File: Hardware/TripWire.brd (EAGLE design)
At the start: 32.3 x 50.2 mm, 56 parts, among them P1 LSP11, P2 LSP11, P3 LSP11, P4 LSP11, P5 LSP11, P6 LSP11, P7 LSP11, X1 GADGETEER-SOCKET

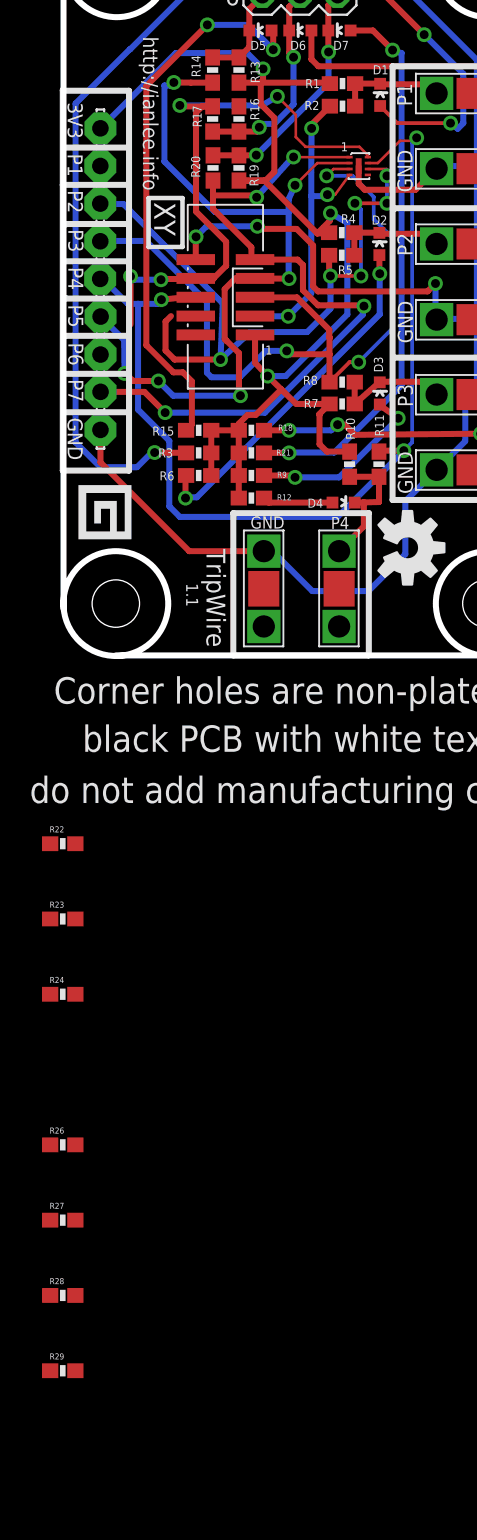
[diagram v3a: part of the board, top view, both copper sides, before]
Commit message: Started replacing TVS with BAT54S diode arrays.
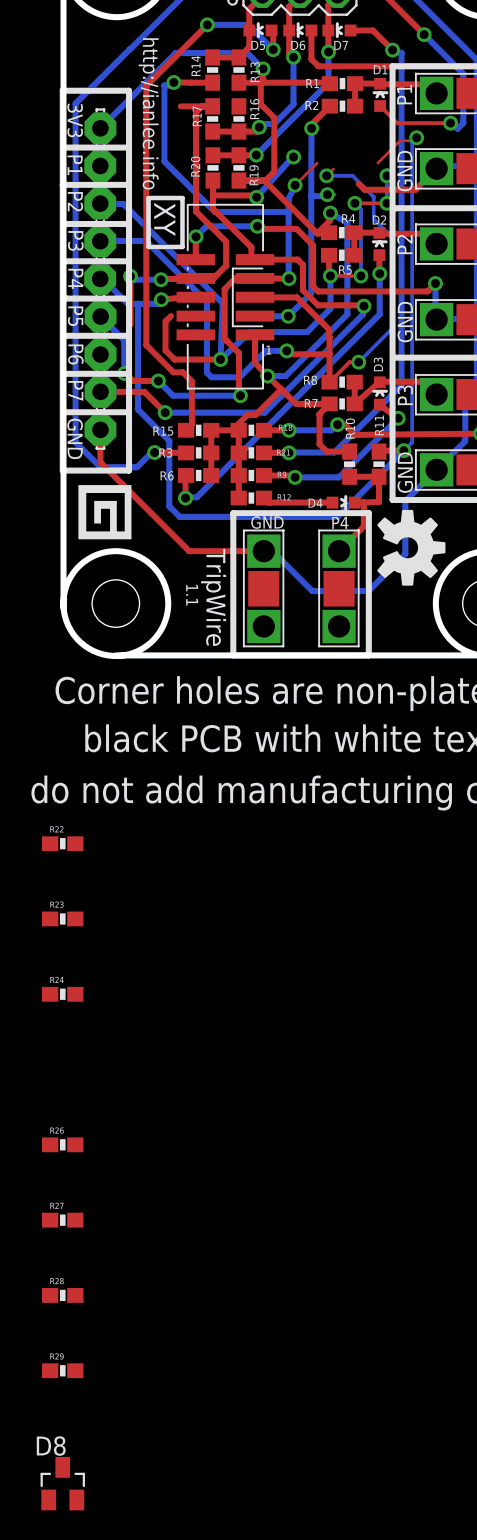
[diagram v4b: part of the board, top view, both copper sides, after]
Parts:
- removed VESD05A8A-HNH-GS08: VESD05A8A-HNH-GS088-UFDFN_TVS-DIODE-ARRAY, SoftDust:8-UFDFN
- added D8: BAT54S, diode:SOT23
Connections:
- net 3V3: now also D8.2
- net GND: now also D8.1; no longer VESD05A8A-HNH-GS08.P$9
- net PIN3: now also D8.3; no longer VESD05A8A-HNH-GS08.P$4
- net PIN4: no longer VESD05A8A-HNH-GS08.P$6
- net PIN5: no longer VESD05A8A-HNH-GS08.P$3
- net PIN6: no longer VESD05A8A-HNH-GS08.P$7
- net PIN7: no longer VESD05A8A-HNH-GS08.P$2
- net PIN8: no longer VESD05A8A-HNH-GS08.P$8
- net PIN9: no longer VESD05A8A-HNH-GS08.P$1
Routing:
- net PIN8: track 41.5 -> 26.0 mm, vias 4 -> 2
- net PIN9: track 16.6 -> 12.9 mm
- net PIN7: track 31.2 -> 29.1 mm
- net PIN3: track 21.2 -> 19.5 mm
- net PIN4: track 46.5 -> 45.3 mm
- net GND: track 117.0 -> 115.8 mm
- net PIN5: track 53.0 -> 52.0 mm
- net PIN6: track 66.7 -> 66.0 mm
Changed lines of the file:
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@@
 <attribute name="VALUE" x="2.295" y="17.7838" size="0.0254" layer="27" rot="R90"/>
 </element>
-<element name="VESD05A8A-HNH-GS08" library="SoftDust" package="8-UFDFN" value="VESD05A8A-HNH-GS088-UFDFN_TVS-DIODE-ARRAY" x="19.9644" y="33.02" smashed="yes"/>
 <element name="LOGO1" library="SparkFun-Aesthetics" package="OSHW-LOGO-M" value="OSHW-LOGOM" x="23.2664" y="7.2644" rot="R270"/>
 <element name="R22" library="SparkFun-Resistors" package="0603-RES" value="10" x="0" y="-12.7"/>
@@
 <element name="R28" library="SparkFun-Resistors" package="0603-RES" value="10" x="0" y="-43.18"/>
 <element name="R29" library="SparkFun-Resistors" package="0603-RES" value="10" x="0" y="-48.26"/>
+<element name="D8" library="diode" package="SOT23" value="BAT54S" x="0" y="-55.88"/>
 </elements>
 <signals>
@@
 <wire x1="13.02035" y1="16.2306" x2="14.7412875" y2="17.9515375" width="0.4064" layer="1"/>
 <wire x1="13.3604" y1="38.647" x2="13.3604" y2="37.1856" width="0.4064" layer="1"/>
+<contactref element="D8" pad="2"/>
+<wire x1="11.8754" y1="10.6172" x2="0.95" y2="-56.98" width="0" layer="19" extent="1-1"/>
 </signal>
 <signal name="GND" class="1">
@@
 <contactref element="SV1" pad="3"/>
 <contactref element="SV1" pad="1"/>
-<contactref element="VESD05A8A-HNH-GS08" pad="P$9"/>
 <wire x1="23.7998" y1="31.4198" x2="25.2222" y2="32.8422" width="0.4064" layer="1"/>
 <wire x1="21.082" y1="47.037" x2="18.542" y2="47.037" width="0.4064" layer="16"/>
@@
 <wire x1="25.2222" y1="22.6568" x2="25.273" y2="22.7076" width="0.4064" layer="16"/>
 <wire x1="25.273" y1="22.7076" x2="27.94" y2="22.7076" width="0.4064" layer="16"/>
-<wire x1="19.9644" y1="33.02" x2="19.9644" y2="31.8262" width="0.4064" layer="1"/>
 <wire x1="19.9644" y1="31.8262" x2="20.3708" y2="31.4198" width="0.4064" layer="1"/>
 <wire x1="20.3708" y1="31.4198" x2="23.7998" y2="31.4198" width="0.4064" layer="1"/>
 <wire x1="25.2222" y1="22.6568" x2="25.146" y2="22.6568" width="0.4064" layer="16"/>
-<wire x1="25.2476" y1="32.8676" x2="25.2222" y2="32.8422" width="0" layer="19" extent="16-16"/>
+<contactref element="D8" pad="1"/>
+<wire x1="16.8402" y1="4.3434" x2="-0.95" y2="-56.98" width="0" layer="19" extent="1-16"/>
+<wire x1="25.2222" y1="32.8422" x2="25.2476" y2="32.8676" width="0" layer="19" extent="16-16"/>
 </signal>
 <signal name="PIN3">
@@
 <wire x1="15.2146" y1="22.8854" x2="15.2038" y2="22.8962" width="0.4064" layer="1"/>
 <wire x1="12.6734" y1="22.8854" x2="15.2146" y2="22.8854" width="0.4064" layer="16"/>
-<contactref element="VESD05A8A-HNH-GS08" pad="P$4"/>
 <via x="17.8562" y="31.0896" extent="1-16" drill="0.6" shape="square"/>
 <wire x1="17.8562" y1="31.0896" x2="17.7546" y2="30.988" width="0.4064" layer="16"/>
 <wire x1="17.7546" y1="30.988" x2="16.764" y2="30.988" width="0.4064" layer="16"/>
 <wire x1="18.3736" y1="31.0896" x2="17.8562" y2="31.0896" width="0.1778" layer="1"/>
-<wire x1="19.3484" y1="32.42" x2="18.3736" y2="31.0896" width="0.1778" layer="1"/>
 <contactref element="R26" pad="1"/>
-<wire x1="-0.85" y1="-33.02" x2="12.6734" y2="22.8854" width="0" layer="19" extent="1-16"/>
+<contactref element="D8" pad="3"/>
+<wire x1="-0.85" y1="-33.02" x2="0" y2="-54.78" width="0" layer="19" extent="1-1"/>
+<wire x1="12.6734" y1="22.8854" x2="-0.85" y2="-33.02" width="0" layer="19" extent="1-16"/>
 </signal>
 <signal name="PIN4">
@@
 <wire x1="16.4846" y1="21.8186" x2="18.0594" y2="23.3934" width="0.4064" layer="16"/>
 <wire x1="18.0594" y1="23.3934" x2="18.0594" y2="25.6032" width="0.4064" layer="16"/>
-<contactref element="VESD05A8A-HNH-GS08" pad="P$6"/>
-<wire x1="20.5844" y1="32.82" x2="21.8662" y2="32.82" width="0.1778" layer="1"/>
 <wire x1="21.8662" y1="32.82" x2="21.8694" y2="32.3596" width="0.1778" layer="1"/>
 <via x="21.8694" y="32.3596" extent="1-16" drill="0.6" shape="square"/>
@@
 <wire x1="17.9832" y1="21.971" x2="17.9832" y2="21.4612" width="0.4064" layer="1"/>
 <wire x1="17.9832" y1="21.4612" x2="18.0086" y2="21.4358" width="0.4064" layer="1"/>
-<contactref element="VESD05A8A-HNH-GS08" pad="P$3"/>
-<wire x1="19.3484" y1="32.82" x2="18.2658" y2="32.82" width="0.1778" layer="1"/>
 <wire x1="18.2658" y1="32.82" x2="17.8054" y2="32.3596" width="0.1778" layer="1"/>
 <via x="17.8054" y="32.3596" extent="1-16" drill="0.6" shape="square"/>
@@
 <wire x1="15.2654" y1="25.4254" x2="12.9836" y2="25.4254" width="0.4064" layer="1"/>
 <wire x1="15.2654" y1="25.4254" x2="15.24" y2="25.4508" width="0.4064" layer="16"/>
-<contactref element="VESD05A8A-HNH-GS08" pad="P$2"/>
-<wire x1="19.3484" y1="33.22" x2="17.1672" y2="33.22" width="0.1778" layer="1"/>
 <via x="15.6718" y="31.7246" extent="1-16" drill="0.6" shape="square"/>
 <wire x1="15.24" y1="25.4508" x2="15.24" y2="29.9212" width="0.4064" layer="16"/>
@@
 <wire x1="10.1346" y1="30.1244" x2="12.7254" y2="27.5336" width="0.4064" layer="1"/>
 <wire x1="12.7254" y1="27.5336" x2="12.7254" y2="26.9536" width="0.4064" layer="1"/>
-<contactref element="VESD05A8A-HNH-GS08" pad="P$1"/>
-<wire x1="19.3484" y1="33.62" x2="15.5798" y2="33.62" width="0.1778" layer="1"/>
 <wire x1="15.5798" y1="33.62" x2="15.5702" y2="33.6296" width="0.4064" layer="1"/>
 <via x="15.5702" y="33.6296" extent="1-16" drill="0.6" shape="square"/>
@@
 <wire x1="7.1882" y1="14.478" x2="5.08" y2="16.5862" width="0.4064" layer="16"/>
 <wire x1="5.08" y1="16.5862" x2="5.08" y2="23.7236" width="0.4064" layer="16"/>
-<contactref element="VESD05A8A-HNH-GS08" pad="P$7"/>
-<wire x1="20.5844" y1="33.22" x2="21.2566" y2="33.22" width="0.1778" layer="1"/>
 <wire x1="21.2566" y1="33.22" x2="22.7584" y2="34.7218" width="0.1778" layer="1"/>
 <wire x1="22.7584" y1="34.7218" x2="23.5458" y2="34.7218" width="0.1778" layer="1"/>
@@
 <wire x1="4.8006" y1="25.3492" x2="6.6294" y2="25.3492" width="0.4064" layer="16"/>
 <wire x1="4.572" y1="22.324" x2="4.572" y2="25.5778" width="0.4064" layer="1"/>
-<contactref element="VESD05A8A-HNH-GS08" pad="P$8"/>
-<via x="14.478" y="37.719" extent="1-16" drill="0.6" shape="square"/>
-<wire x1="14.478" y1="37.719" x2="13.4366" y2="37.1094" width="0.4064" layer="16"/>
-<wire x1="13.4366" y1="37.1094" x2="7.8994" y2="37.1094" width="0.4064" layer="16"/>
-<via x="7.8994" y="37.1094" extent="1-16" drill="0.6" shape="square"/>
 <wire x1="7.9638" y1="37.045" x2="10.1092" y2="37.045" width="0.4064" layer="1"/>
-<wire x1="14.478" y1="37.719" x2="15.7226" y2="36.4744" width="0.1778" layer="1"/>
-<wire x1="15.7226" y1="36.4744" x2="15.7226" y2="34.9758" width="0.1778" layer="1"/>
-<wire x1="15.7226" y1="34.9758" x2="16.383" y2="34.3154" width="0.1778" layer="1"/>
-<wire x1="16.383" y1="34.3154" x2="20.0152" y2="34.3154" width="0.1778" layer="1"/>
-<wire x1="20.0152" y1="34.3154" x2="20.5844" y2="33.7462" width="0.1778" layer="1"/>
-<wire x1="20.5844" y1="33.7462" x2="20.5844" y2="33.62" width="0.1778" layer="1"/>
 <wire x1="6.7056" y1="25.4" x2="10.16" y2="25.4" width="0.4064" layer="1"/>
 <wire x1="10.16" y1="25.4" x2="10.16" y2="25.4254" width="0.4064" layer="1"/>
 <contactref element="R24" pad="2"/>
-<wire x1="7.9638" y1="37.045" x2="7.8994" y2="37.1094" width="0" layer="19" extent="1-16"/>
 <wire x1="0.85" y1="-22.86" x2="4.572" y2="22.324" width="0" layer="19" extent="1-1"/>
 </signal>

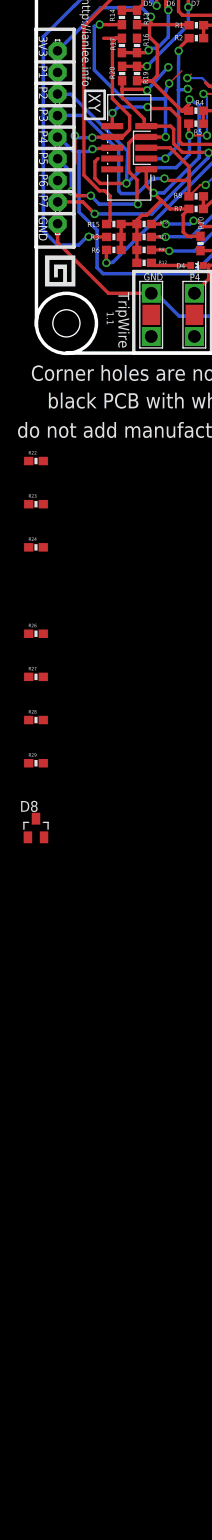
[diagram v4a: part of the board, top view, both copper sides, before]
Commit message: Downgraded to Eagle 6.1.0.  Added Schottky circuit protection and signal filtering capacitors.
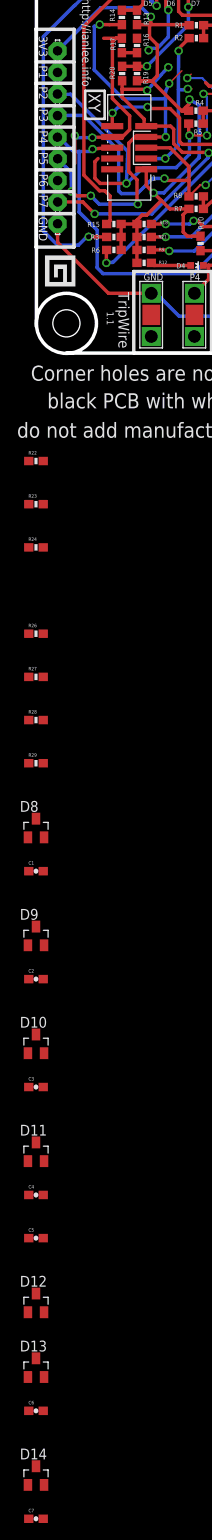
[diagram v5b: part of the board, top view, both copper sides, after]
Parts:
- added C1, C2, C3, C4, C5, C6, C7: 0.01 uF, SparkFun-Capacitors:0603-CAP
- added D10, D11, D12, D13, D14, D9: BAT54S, diode:SOT23
- R1, R10, R13, R16, R19, R4, R7: value 10K -> 100K
- R11, R14, R17, R2, R20, R5, R8: value 100 -> 1K
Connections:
- new net N$23: C6.1, R16.2, R17.2
- net 3V3: now also D10.2, D11.2, D12.2, D13.2, D14.2, D9.2
- net GND: now also C1.2, C2.2, C3.2, C4.2, C5.2, C6.2, C7.2, D10.1, D11.1, D12.1, D13.1, D14.1, D9.1
- net N$11: now also C1.1
- net N$14: now also C5.1
- net N$2: now also C3.1
- net N$4: now also C2.1
- net N$6: now also C7.1
- net N$8: now also C4.1
- net N$9: no longer R16.2, R17.2
- net PIN4: now also D10.3
- net PIN5: now also D9.3
- net PIN6: now also D11.3
- net PIN7: now also D12.3
- net PIN8: now also D13.3
- net PIN9: now also D14.3
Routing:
- net N$9: track 14.1 -> 11.1 mm
- net N$23: track 0.00 -> 1.78 mm
